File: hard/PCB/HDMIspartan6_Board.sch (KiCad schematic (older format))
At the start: 50 parts

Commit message: Update supply power
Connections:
- wire segments 17 -> 18
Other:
- note added: "PENDIENTES:\n\n>>> IMPLEMENTAR REGLAS DEL FABRICANTE <<<\n\n- Reorganizar PinOut\n- Asignar LEDs indicadores a FPGA\n"
- note removed: "PENDIENTES:\n\n>>> IMPLEMENTAR REGLAS DEL FABRICANTE <<<\n\n- Reorganizar PinOut\n- Asignar LEDs indicadores a FPGA\n\n\nDUDAS:\n\n- El pin ~SD~ del amplificador de sonido PAM8302 esta conectado\n desde la FPGA para habilitar el sonido, pero tambien a una \nregleta para poder activilarlo con un jumper ¿se requiere alguna\ncomponente adicional para porteger el amplificar y la FPGA?\nCaso hipotetic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"
- moved on the sheet: TH1, TH10, TH11, TH12, TH13, TH14, TH15, TH16, TH17, TH18, TH19, TH2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

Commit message: Corrección esquematico
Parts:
- TH1, TH10, TH11, TH12, TH13, TH14, TH15, TH16, TH17, TH18, TH19, TH2, TH20, TH21, TH22, TH23, TH24, TH25, TH26, TH27, TH28, TH29, TH3, TH30, TH31, TH32, TH33, TH34, TH35, TH36, TH37, TH38, TH39, TH4, TH40, TH41, TH42, TH43, TH44, TH45, TH46, TH47, TH48, TH49, TH5, TH50, TH6, TH7, TH8, TH9: footprint opendous:1Pin_12mil_VIA -> Project:1Pin_12mil_VIA

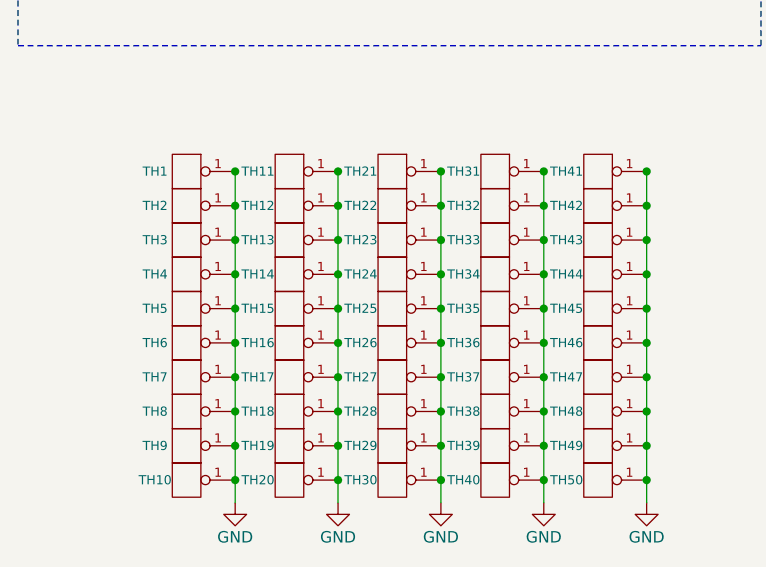
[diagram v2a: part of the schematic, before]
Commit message: update 3d models
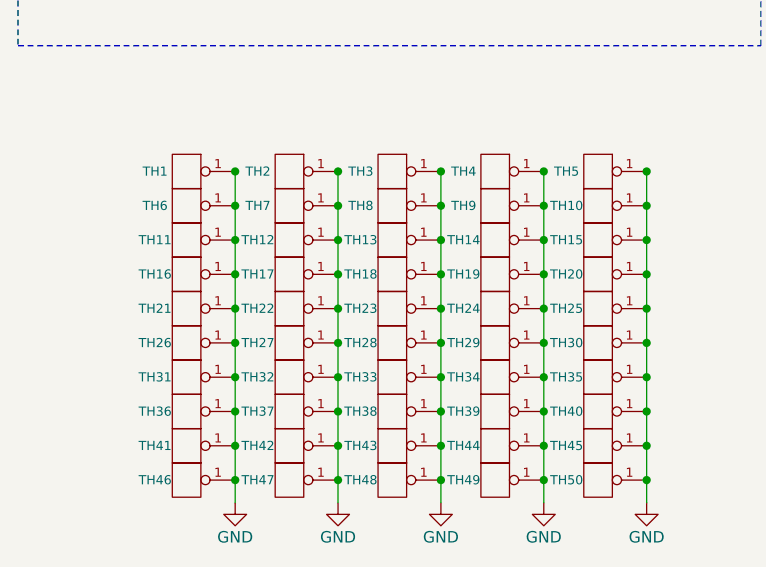
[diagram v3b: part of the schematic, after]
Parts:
- renumbered TH42 to TH10, TH3 to TH11, TH13 to TH12, TH23 to TH13, TH33 to TH14, TH43 to TH15, TH4 to TH16, TH14 to TH17, TH24 to TH18, TH34 to TH19, TH11 to TH2, TH44 to TH20, TH5 to TH21, TH15 to TH22, TH25 to TH23, TH35 to TH24, TH45 to TH25, TH6 to TH26, TH16 to TH27, TH26 to TH28, TH36 to TH29, TH21 to TH3, TH46 to TH30, TH7 to TH31, TH17 to TH32, TH27 to TH33, TH37 to TH34, TH47 to TH35, TH8 to TH36, TH18 to TH37, TH28 to TH38, TH38 to TH39, TH31 to TH4, TH48 to TH40, TH9 to TH41, TH19 to TH42, TH29 to TH43, TH39 to TH44, TH49 to TH45, TH10 to TH46, TH20 to TH47, TH30 to TH48, TH40 to TH49, TH41 to TH5, TH2 to TH6, TH12 to TH7, TH22 to TH8, TH32 to TH9

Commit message: update layout
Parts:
- renumbered TH21 to TH22, TH22 to TH23, TH23 to TH24, TH24 to TH25, TH25 to TH26, TH26 to TH28, TH27 to TH29, TH28 to TH30, TH29 to TH31, TH30 to TH32, TH31 to TH34, TH32 to TH35, TH33 to TH36, TH34 to TH37, TH35 to TH38, TH36 to TH40, TH37 to TH41, TH38 to TH42, TH39 to TH43, TH40 to TH44, TH41 to TH45, TH42 to TH46, TH43 to TH47, TH44 to TH48, TH45 to TH49, TH46 to TH50, TH47 to TH51, TH48 to TH52, TH49 to TH53, TH50 to TH54
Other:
- moved on the sheet: TH1, TH10, TH11, TH12, TH13, TH14, TH15, TH16, TH17, TH18, TH19, TH2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

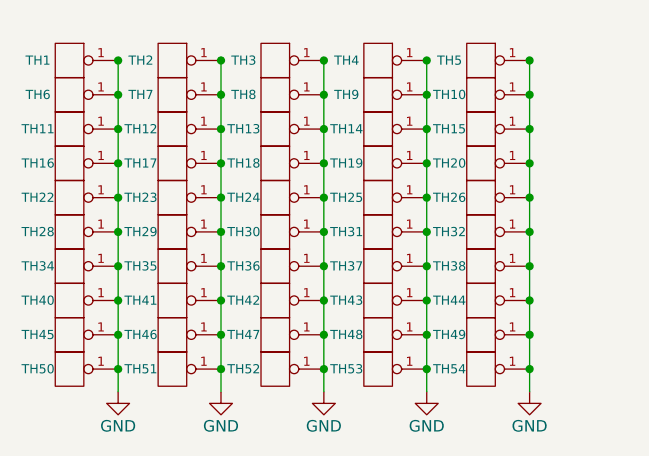
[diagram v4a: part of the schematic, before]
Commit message: Add jmp Rpi Power
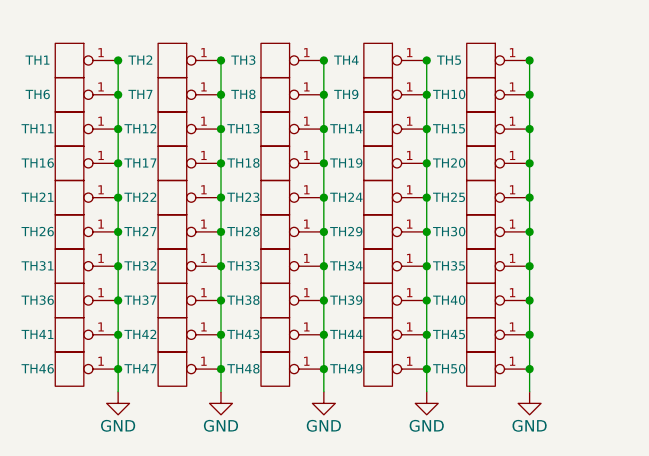
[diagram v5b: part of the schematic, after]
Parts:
- renumbered TH22 to TH21, TH23 to TH22, TH24 to TH23, TH25 to TH24, TH26 to TH25, TH28 to TH26, TH29 to TH27, TH30 to TH28, TH31 to TH29, TH32 to TH30, TH34 to TH31, TH35 to TH32, TH36 to TH33, TH37 to TH34, TH38 to TH35, TH40 to TH36, TH41 to TH37, TH42 to TH38, TH43 to TH39, TH44 to TH40, TH45 to TH41, TH46 to TH42, TH47 to TH43, TH48 to TH44, TH49 to TH45, TH50 to TH46, TH51 to TH47, TH52 to TH48, TH53 to TH49, TH54 to TH50
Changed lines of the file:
@@
 $EndSheet
 $Comp
-L GND #PWR01
+L GND #PWR5
 U 1 1 592F8C7B
 P 3400 7500
-F 0 "#PWR01" H 3400 7250 50  0001 C CNN
+F 0 "#PWR5" H 3400 7250 50  0001 C CNN
 F 1 "GND" H 3400 7350 50  0000 C CNN
 F 2 "" H 3400 7500 50  0001 C CNN
@@
 $EndComp
 $Comp
-L GND #PWR02
+L GND #PWR4
 U 1 1 592F918E
 P 2950 7500
-F 0 "#PWR02" H 2950 7250 50  0001 C CNN
+F 0 "#PWR4" H 2950 7250 50  0001 C CNN
 F 1 "GND" H 2950 7350 50  0000 C CNN
 F 2 "" H 2950 7500 50  0001 C CNN
@@
 $EndComp
 $Comp
-L GND #PWR03
+L GND #PWR3
 U 1 1 592F9238
 P 2500 7500
-F 0 "#PWR03" H 2500 7250 50  0001 C CNN
+F 0 "#PWR3" H 2500 7250 50  0001 C CNN
 F 1 "GND" H 2500 7350 50  0000 C CNN
 F 2 "" H 2500 7500 50  0001 C CNN
@@
 $EndComp
 $Comp
-L GND #PWR04
+L GND #PWR2
 U 1 1 592F92E2
 P 2050 7500
-F 0 "#PWR04" H 2050 7250 50  0001 C CNN
+F 0 "#PWR2" H 2050 7250 50  0001 C CNN
 F 1 "GND" H 2050 7350 50  0000 C CNN
 F 2 "" H 2050 7500 50  0001 C CNN
@@
 $EndComp
 $Comp
-L GND #PWR05
+L GND #PWR1
 U 1 1 592F938C
 P 1600 7500
-F 0 "#PWR05" H 1600 7250 50  0001 C CNN
+F 0 "#PWR1" H 1600 7250 50  0001 C CNN
 F 1 "GND" H 1600 7350 50  0000 C CNN
 F 2 "" H 1600 7500 50  0001 C CNN
@@
 $EndComp
 $Comp
-L CONN_1 TH22
+L CONN_1 TH21
 U 1 1 592FC288
 P 1350 6650
-F 0 "TH22" H 1250 6650 40  0000 C CNN
+F 0 "TH21" H 1250 6650 40  0000 C CNN
 F 1 "CONN_1" H 1450 6550 40  0001 C CNN
 F 2 "Project:1Pin_12mil_VIA" H 1350 6650 30  0001 C CNN
@@
 $EndComp
 $Comp
-L CONN_1 TH28
+L CONN_1 TH26
 U 1 1 592FC28E
 P 1350 6800
-F 0 "TH28" H 1250 6800 40  0000 C CNN
+F 0 "TH26" H 1250 6800 40  0000 C CNN
 F 1 "CONN_1" H 1450 6700 40  0001 C CNN
 F 2 "Project:1Pin_12mil_VIA" H 1350 6800 30  0001 C CNN
@@
 $EndComp
 $Comp
-L CONN_1 TH34
+L CONN_1 TH31
 U 1 1 592FC480
 P 1350 6950
-F 0 "TH34" H 1250 6950 40  0000 C CNN
+F 0 "TH31" H 1250 6950 40  0000 C CNN
 F 1 "CONN_1" H 1450 6850 40  0001 C CNN
 F 2 "Project:1Pin_12mil_VIA" H 1350 6950 30  0001 C CNN
@@
 $EndComp
 $Comp
-L CONN_1 TH40
+L CONN_1 TH36
 U 1 1 592FC486
 P 1350 7100
-F 0 "TH40" H 1250 7100 40  0000 C CNN
+F 0 "TH36" H 1250 7100 40  0000 C CNN
 F 1 "CONN_1" H 1450 7000 40  0001 C CNN
 F 2 "Project:1Pin_12mil_VIA" H 1350 7100 30  0001 C CNN
@@
 $EndComp
 $Comp
-L CONN_1 TH45
+L CONN_1 TH41
 U 1 1 592FC48C
 P 1350 7250
-F 0 "TH45" H 1250 7250 40  0000 C CNN
+F 0 "TH41" H 1250 7250 40  0000 C CNN
 F 1 "CONN_1" H 1450 7150 40  0001 C CNN
 F 2 "Project:1Pin_12mil_VIA" H 1350 7250 30  0001 C CNN
@@
 $EndComp
 $Comp
-L CONN_1 TH50
+L CONN_1 TH46
 U 1 1 592FC492
 P 1350 7400
-F 0 "TH50" H 1250 7400 40  0000 C CNN
+F 0 "TH46" H 1250 7400 40  0000 C CNN
 F 1 "CONN_1" H 1450 7300 40  0001 C CNN
 F 2 "Project:1Pin_12mil_VIA" H 1350 7400 30  0001 C CNN
@@
 $EndComp
 $Comp
-L CONN_1 TH23
+L CONN_1 TH22
 U 1 1 592FD36C
 P 1800 6650
-F 0 "TH23" H 1700 6650 40  0000 C CNN
+F 0 "TH22" H 1700 6650 40  0000 C CNN
 F 1 "CONN_1" H 1900 6550 40  0001 C CNN
 F 2 "Project:1Pin_12mil_VIA" H 1800 6650 30  0001 C CNN
@@
 $EndComp
 $Comp
-L CONN_1 TH29
+L CONN_1 TH27
 U 1 1 592FD372
 P 1800 6800
-F 0 "TH29" H 1700 6800 40  0000 C CNN
+F 0 "TH27" H 1700 6800 40  0000 C CNN
 F 1 "CONN_1" H 1900 6700 40  0001 C CNN
 F 2 "Project:1Pin_12mil_VIA" H 1800 6800 30  0001 C CNN
@@
 $EndComp
 $Comp
-L CONN_1 TH35
+L CONN_1 TH32
 U 1 1 592FD378
 P 1800 6950
-F 0 "TH35" H 1700 6950 40  0000 C CNN
+F 0 "TH32" H 1700 6950 40  0000 C CNN
 F 1 "CONN_1" H 1900 6850 40  0001 C CNN
 F 2 "Project:1Pin_12mil_VIA" H 1800 6950 30  0001 C CNN
@@
 $EndComp
 $Comp
-L CONN_1 TH41
+L CONN_1 TH37
 U 1 1 592FD37E
 P 1800 7100
-F 0 "TH41" H 1700 7100 40  0000 C CNN
+F 0 "TH37" H 1700 7100 40  0000 C CNN
 F 1 "CONN_1" H 1900 7000 40  0001 C CNN
 F 2 "Project:1Pin_12mil_VIA" H 1800 7100 30  0001 C CNN
@@
 $EndComp
 $Comp
-L CONN_1 TH46
+L CONN_1 TH42
 U 1 1 592FD384
 P 1800 7250
-F 0 "TH46" H 1700 7250 40  0000 C CNN
+F 0 "TH42" H 1700 7250 40  0000 C CNN
 F 1 "CONN_1" H 1900 7150 40  0001 C CNN
 F 2 "Project:1Pin_12mil_VIA" H 1800 7250 30  0001 C CNN
@@
 $EndComp
 $Comp
-L CONN_1 TH51
+L CONN_1 TH47
 U 1 1 592FD38A
 P 1800 7400
-F 0 "TH51" H 1700 7400 40  0000 C CNN
+F 0 "TH47" H 1700 7400 40  0000 C CNN
 F 1 "CONN_1" H 1900 7300 40  0001 C CNN
 F 2 "Project:1Pin_12mil_VIA" H 1800 7400 30  0001 C CNN
@@
 $EndComp
 $Comp
-L CONN_1 TH24
+L CONN_1 TH23
 U 1 1 592FD7AA
 P 2250 6650
-F 0 "TH24" H 2150 6650 40  0000 C CNN
+F 0 "TH23" H 2150 6650 40  0000 C CNN
 F 1 "CONN_1" H 2350 6550 40  0001 C CNN
 F 2 "Project:1Pin_12mil_VIA" H 2250 6650 30  0001 C CNN
@@
 $EndComp
 $Comp
-L CONN_1 TH30
+L CONN_1 TH28
 U 1 1 592FD7B0
 P 2250 6800
-F 0 "TH30" H 2150 6800 40  0000 C CNN
+F 0 "TH28" H 2150 6800 40  0000 C CNN
 F 1 "CONN_1" H 2350 6700 40  0001 C CNN
 F 2 "Project:1Pin_12mil_VIA" H 2250 6800 30  0001 C CNN
@@
 $EndComp
 $Comp
-L CONN_1 TH36
+L CONN_1 TH33
 U 1 1 592FD7B6
 P 2250 6950
-F 0 "TH36" H 2150 6950 40  0000 C CNN
+F 0 "TH33" H 2150 6950 40  0000 C CNN
 F 1 "CONN_1" H 2350 6850 40  0001 C CNN
 F 2 "Project:1Pin_12mil_VIA" H 2250 6950 30  0001 C CNN
@@
 $EndComp
 $Comp
-L CONN_1 TH42
+L CONN_1 TH38
 U 1 1 592FD7BC
 P 2250 7100
-F 0 "TH42" H 2150 7100 40  0000 C CNN
+F 0 "TH38" H 2150 7100 40  0000 C CNN
 F 1 "CONN_1" H 2350 7000 40  0001 C CNN
 F 2 "Project:1Pin_12mil_VIA" H 2250 7100 30  0001 C CNN
@@
 $EndComp
 $Comp
-L CONN_1 TH47
+L CONN_1 TH43
 U 1 1 592FD7C2
 P 2250 7250
-F 0 "TH47" H 2150 7250 40  0000 C CNN
+F 0 "TH43" H 2150 7250 40  0000 C CNN
 F 1 "CONN_1" H 2350 7150 40  0001 C CNN
 F 2 "Project:1Pin_12mil_VIA" H 2250 7250 30  0001 C CNN
@@
 $EndComp
 $Comp
-L CONN_1 TH52
+L CONN_1 TH48
 U 1 1 592FD7C8
 P 2250 7400
-F 0 "TH52" H 2150 7400 40  0000 C CNN
+F 0 "TH48" H 2150 7400 40  0000 C CNN
 F 1 "CONN_1" H 2350 7300 40  0001 C CNN
 F 2 "Project:1Pin_12mil_VIA" H 2250 7400 30  0001 C CNN
@@
 $EndComp
 $Comp
-L CONN_1 TH25
+L CONN_1 TH24
 U 1 1 592FDA7E
 P 2700 6650
-F 0 "TH25" H 2600 6650 40  0000 C CNN
+F 0 "TH24" H 2600 6650 40  0000 C CNN
 F 1 "CONN_1" H 2800 6550 40  0001 C CNN
 F 2 "Project:1Pin_12mil_VIA" H 2700 6650 30  0001 C CNN
@@
 $EndComp
 $Comp
-L CONN_1 TH31
+L CONN_1 TH29
 U 1 1 592FDA84
 P 2700 6800
-F 0 "TH31" H 2600 6800 40  0000 C CNN
+F 0 "TH29" H 2600 6800 40  0000 C CNN
 F 1 "CONN_1" H 2800 6700 40  0001 C CNN
 F 2 "Project:1Pin_12mil_VIA" H 2700 6800 30  0001 C CNN
@@
 $EndComp
 $Comp
-L CONN_1 TH37
+L CONN_1 TH34
 U 1 1 592FDA8A
 P 2700 6950
-F 0 "TH37" H 2600 6950 40  0000 C CNN
+F 0 "TH34" H 2600 6950 40  0000 C CNN
 F 1 "CONN_1" H 2800 6850 40  0001 C CNN
 F 2 "Project:1Pin_12mil_VIA" H 2700 6950 30  0001 C CNN
@@
 $EndComp
 $Comp
-L CONN_1 TH43
+L CONN_1 TH39
 U 1 1 592FDA90
 P 2700 7100
-F 0 "TH43" H 2600 7100 40  0000 C CNN
+F 0 "TH39" H 2600 7100 40  0000 C CNN
 F 1 "CONN_1" H 2800 7000 40  0001 C CNN
 F 2 "Project:1Pin_12mil_VIA" H 2700 7100 30  0001 C CNN
@@
 $EndComp
 $Comp
-L CONN_1 TH48
+L CONN_1 TH44
 U 1 1 592FDA96
 P 2700 7250
-F 0 "TH48" H 2600 7250 40  0000 C CNN
+F 0 "TH44" H 2600 7250 40  0000 C CNN
 F 1 "CONN_1" H 2800 7150 40  0001 C CNN
 F 2 "Project:1Pin_12mil_VIA" H 2700 7250 30  0001 C CNN
@@
 $EndComp
 $Comp
-L CONN_1 TH53
+L CONN_1 TH49
 U 1 1 592FDA9C
 P 2700 7400
-F 0 "TH53" H 2600 7400 40  0000 C CNN
+F 0 "TH49" H 2600 7400 40  0000 C CNN
 F 1 "CONN_1" H 2800 7300 40  0001 C CNN
 F 2 "Project:1Pin_12mil_VIA" H 2700 7400 30  0001 C CNN
@@
 $EndComp
 $Comp
-L CONN_1 TH26
+L CONN_1 TH25
 U 1 1 592FDCE4
 P 3150 6650
-F 0 "TH26" H 3050 6650 40  0000 C CNN
+F 0 "TH25" H 3050 6650 40  0000 C CNN
 F 1 "CONN_1" H 3250 6550 40  0001 C CNN
 F 2 "Project:1Pin_12mil_VIA" H 3150 6650 30  0001 C CNN
@@
 $EndComp
 $Comp
-L CONN_1 TH32
+L CONN_1 TH30
 U 1 1 592FDCEA
 P 3150 6800
-F 0 "TH32" H 3050 6800 40  0000 C CNN
+F 0 "TH30" H 3050 6800 40  0000 C CNN
 F 1 "CONN_1" H 3250 6700 40  0001 C CNN
 F 2 "Project:1Pin_12mil_VIA" H 3150 6800 30  0001 C CNN
@@
 $EndComp
 $Comp
-L CONN_1 TH38
+L CONN_1 TH35
 U 1 1 592FDCF0
 P 3150 6950
-F 0 "TH38" H 3050 6950 40  0000 C CNN
+F 0 "TH35" H 3050 6950 40  0000 C CNN
 F 1 "CONN_1" H 3250 6850 40  0001 C CNN
 F 2 "Project:1Pin_12mil_VIA" H 3150 6950 30  0001 C CNN
@@
 $EndComp
 $Comp
-L CONN_1 TH44
+L CONN_1 TH40
 U 1 1 592FDCF6
 P 3150 7100
-F 0 "TH44" H 3050 7100 40  0000 C CNN
+F 0 "TH40" H 3050 7100 40  0000 C CNN
 F 1 "CONN_1" H 3250 7000 40  0001 C CNN
 F 2 "Project:1Pin_12mil_VIA" H 3150 7100 30  0001 C CNN
@@
 $EndComp
 $Comp
-L CONN_1 TH49
+L CONN_1 TH45
 U 1 1 592FDCFC
 P 3150 7250
-F 0 "TH49" H 3050 7250 40  0000 C CNN
+F 0 "TH45" H 3050 7250 40  0000 C CNN
 F 1 "CONN_1" H 3250 7150 40  0001 C CNN
 F 2 "Project:1Pin_12mil_VIA" H 3150 7250 30  0001 C CNN
@@
 $EndComp
 $Comp
-L CONN_1 TH54
+L CONN_1 TH50
 U 1 1 592FDD02
 P 3150 7400
-F 0 "TH54" H 3050 7400 40  0000 C CNN
+F 0 "TH50" H 3050 7400 40  0000 C CNN
 F 1 "CONN_1" H 3250 7300 40  0001 C CNN
 F 2 "Project:1Pin_12mil_VIA" H 3150 7400 30  0001 C CNN

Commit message: se modifican el pin hdmi- las resitencias RN1 - eñ conector de  voltaje
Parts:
- TH1, TH50: footprint Project:1Pin_12mil_VIA -> Measurement_Points:Measurement_Point_Round-TH_Small
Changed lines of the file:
@@
 F 0 "TH1" H 1250 6050 40  0000 C CNN
 F 1 "CONN_1" H 1450 5950 40  0001 C CNN
-F 2 "Project:1Pin_12mil_VIA" H 1350 6050 30  0001 C CNN
+F 2 "Measurement_Points:Measurement_Point_Round-TH_Small" H 1350 6050 30  0001 C CNN
 F 3 "" H 1350 6050 60  0000 C CNN
 	1    1350 6050
@@
 F 0 "TH50" H 3050 7400 40  0000 C CNN
 F 1 "CONN_1" H 3250 7300 40  0001 C CNN
-F 2 "Project:1Pin_12mil_VIA" H 3150 7400 30  0001 C CNN
+F 2 "Measurement_Points:Measurement_Point_Round-TH_Small" H 3150 7400 30  0001 C CNN
 F 3 "" H 3150 7400 60  0000 C CNN
 	1    3150 7400

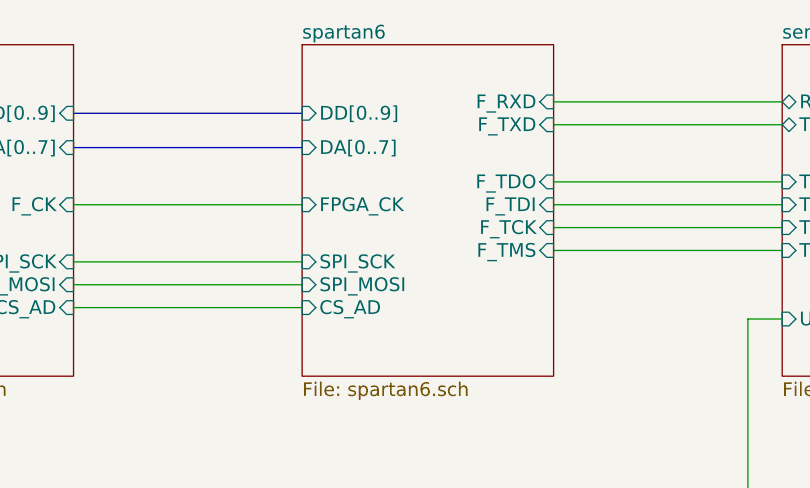
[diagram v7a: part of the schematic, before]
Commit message: ok lvds  and hdmi
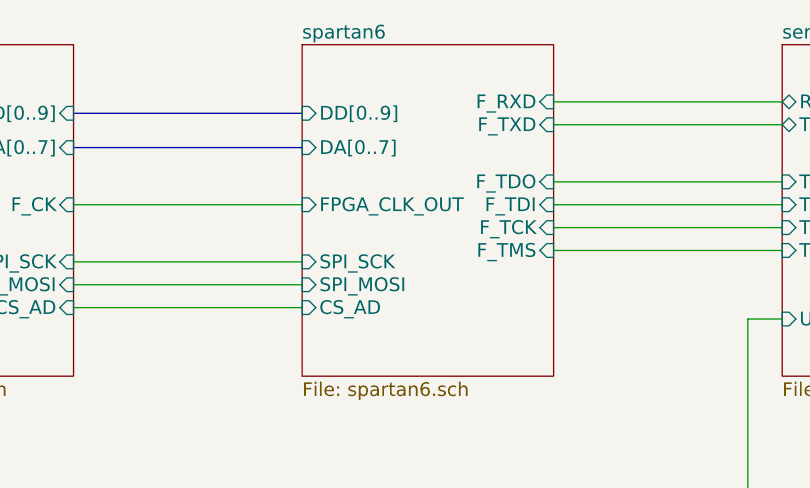
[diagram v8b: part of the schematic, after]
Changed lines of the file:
@@
 F11 "SPI_MOSI" I L 5300 3000 60
 F12 "CS_AD" I L 5300 3100 60
-F13 "FPGA_CK" I L 5300 2650 60
+F13 "FPGA_CLK_OUT" I L 5300 2650 60
 $EndSheet
 $Sheet
